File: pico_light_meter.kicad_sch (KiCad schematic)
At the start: 5 parts

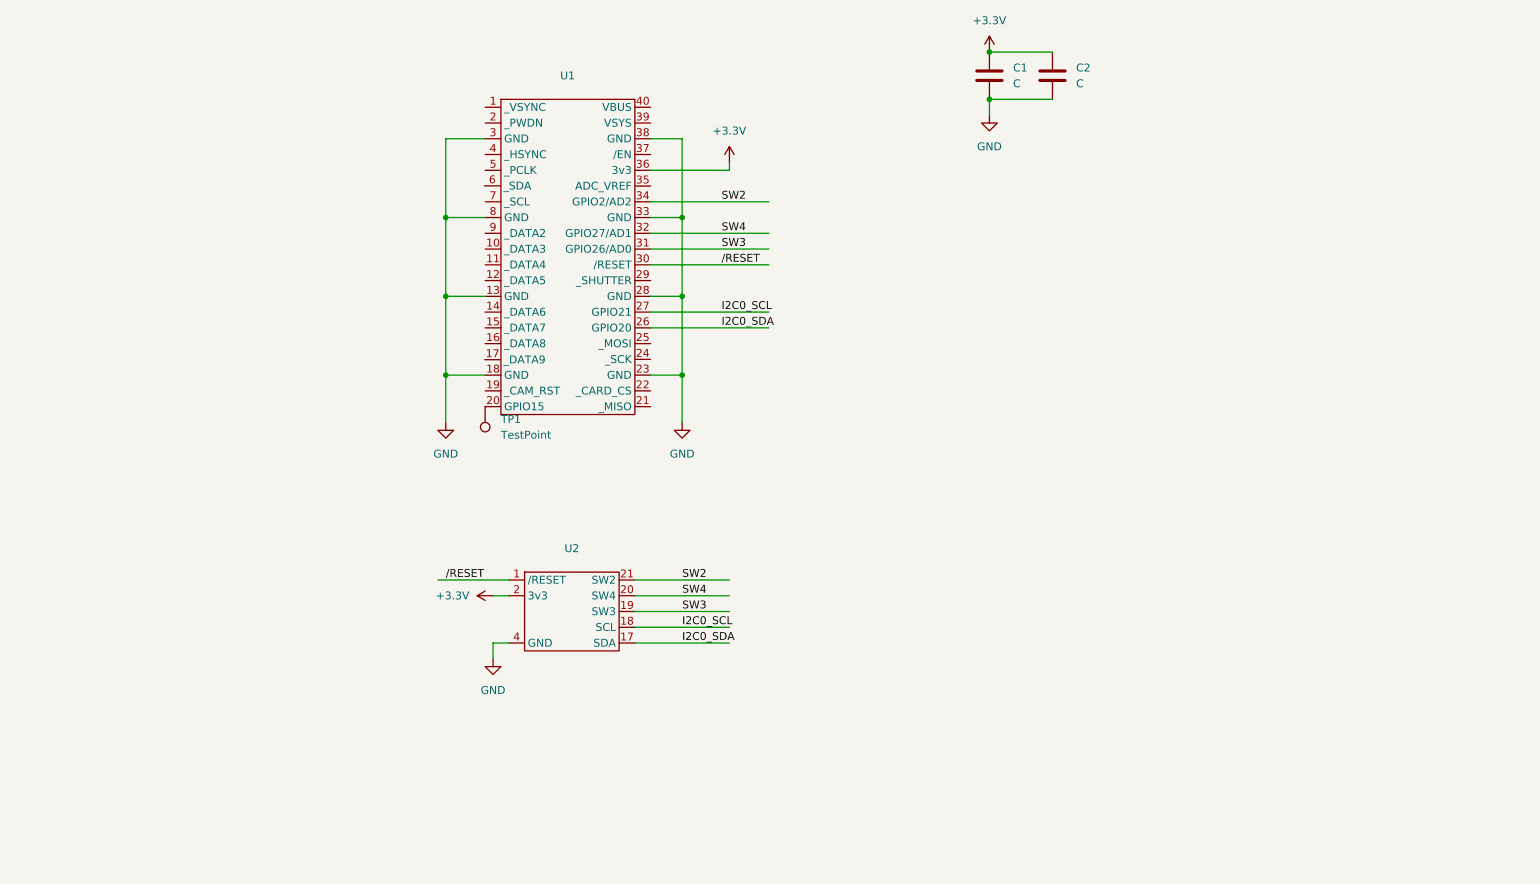
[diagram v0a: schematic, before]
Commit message: Intermediate commit of routed board with Pico on top.
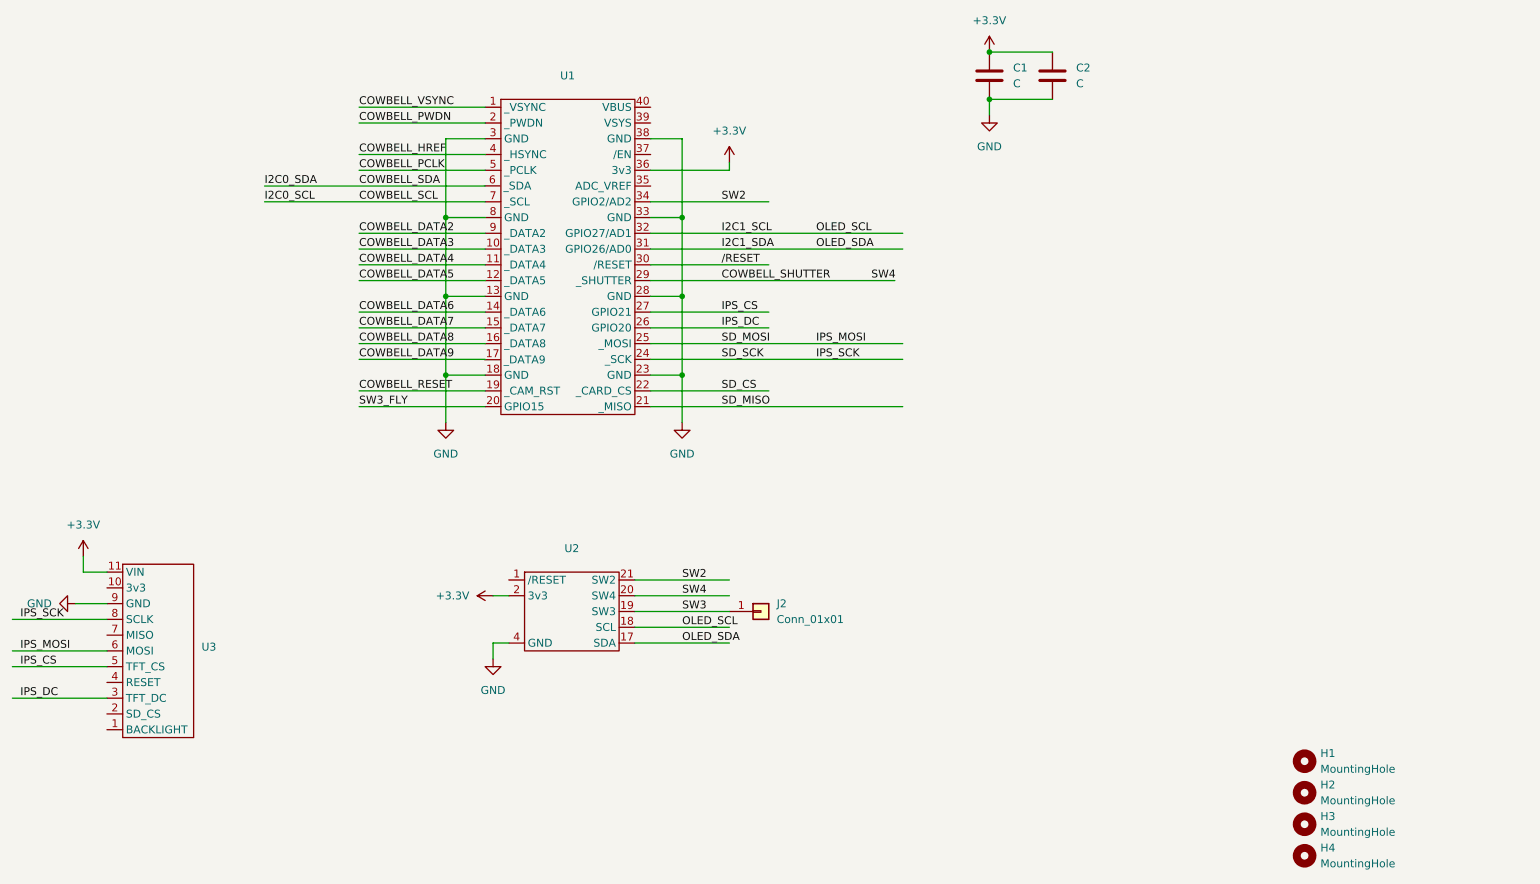
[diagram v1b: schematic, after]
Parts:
- removed TP1: TestPoint, TestPoint:TestPoint_THTPad_D2.0mm_Drill1.0mm, symbol Connector:TestPoint
- added H1, H2, H3, H4: MountingHole, MountingHole:MountingHole_3.2mm_M3_ISO14580, symbol Mechanical:MountingHole
- added J2: Conn_01x01, Connector_PinHeader_1.27mm:PinHeader_1x01_P1.27mm_Vertical, symbol Connector_Generic:Conn_01x01
- added U3: ~, pico_light_meter:adafruit_2.0_IPS_Display, symbol pico_light_meter:Adafruit_2.0_IPS_Display
- U1: footprint pico_light_meter:pico2 -> pico_light_meter:pico2_right_pins_only
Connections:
- net +3.3V: now also U3.11 (VIN)
- net GND: now also U3.9 (GND)
- net SW3: now also J2.1 (Pin_1); no longer U1.31 (GPIO26/AD0)
- net /RESET: no longer U2.1 (/RESET)
- net COWBELL_VSYNC: now reaches U1.1 (_VSYNC)
- net COWBELL_DATA3: now reaches U1.10 (_DATA3)
- net COWBELL_DATA4: now reaches U1.11 (_DATA4)
- net COWBELL_DATA5: now reaches U1.12 (_DATA5)
- net COWBELL_DATA6: now reaches U1.14 (_DATA6)
- net COWBELL_DATA7: now reaches U1.15 (_DATA7)
- net COWBELL_DATA8: now reaches U1.16 (_DATA8)
- net COWBELL_RESET: now reaches U1.19 (_CAM_RST)
- net COWBELL_PWDN: now reaches U1.2 (_PWDN)
- net SW3_FLY: now reaches U1.20 (GPIO15)
- net SD_MISO: now reaches U1.21 (_MISO)
- net SD_CS: now reaches U1.22 (_CARD_CS)
- net IPS_SCK: now reaches U1.24 (_SCK)
- net IPS_SCK: now also U3.8 (SCLK)
- net IPS_MOSI: now reaches U1.25 (_MOSI)
- net IPS_MOSI: now also U3.6 (MOSI)
- net COWBELL_SHUTTER: now reaches U1.29 (_SHUTTER)
- net COWBELL_SHUTTER: now also U2.20 (SW4)
- net COWBELL_HREF: now reaches U1.4 (_HSYNC)
- net COWBELL_PCLK: now reaches U1.5 (_PCLK)
- net COWBELL_SCL: now reaches U1.7 (_SCL)
- net COWBELL_DATA2: now reaches U1.9 (_DATA2)
- net I2C0_SCL renamed I2C1_SCL
- net I2C1_SCL: now also U1.32 (GPIO27/AD1); no longer U1.27 (GPIO21)
- net I2C0_SDA renamed I2C1_SDA
- net I2C1_SDA: now also U1.31 (GPIO26/AD0); no longer U1.26 (GPIO20)
- removed net SW4: U1.32 (GPIO27/AD1), U2.20 (SW4)
- new net IPS_CS: U1.27 (GPIO21), U3.5 (TFT_CS)
- new net IPS_DC: U1.26 (GPIO20), U3.3 (TFT_DC)

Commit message: Updated with MCP port expander
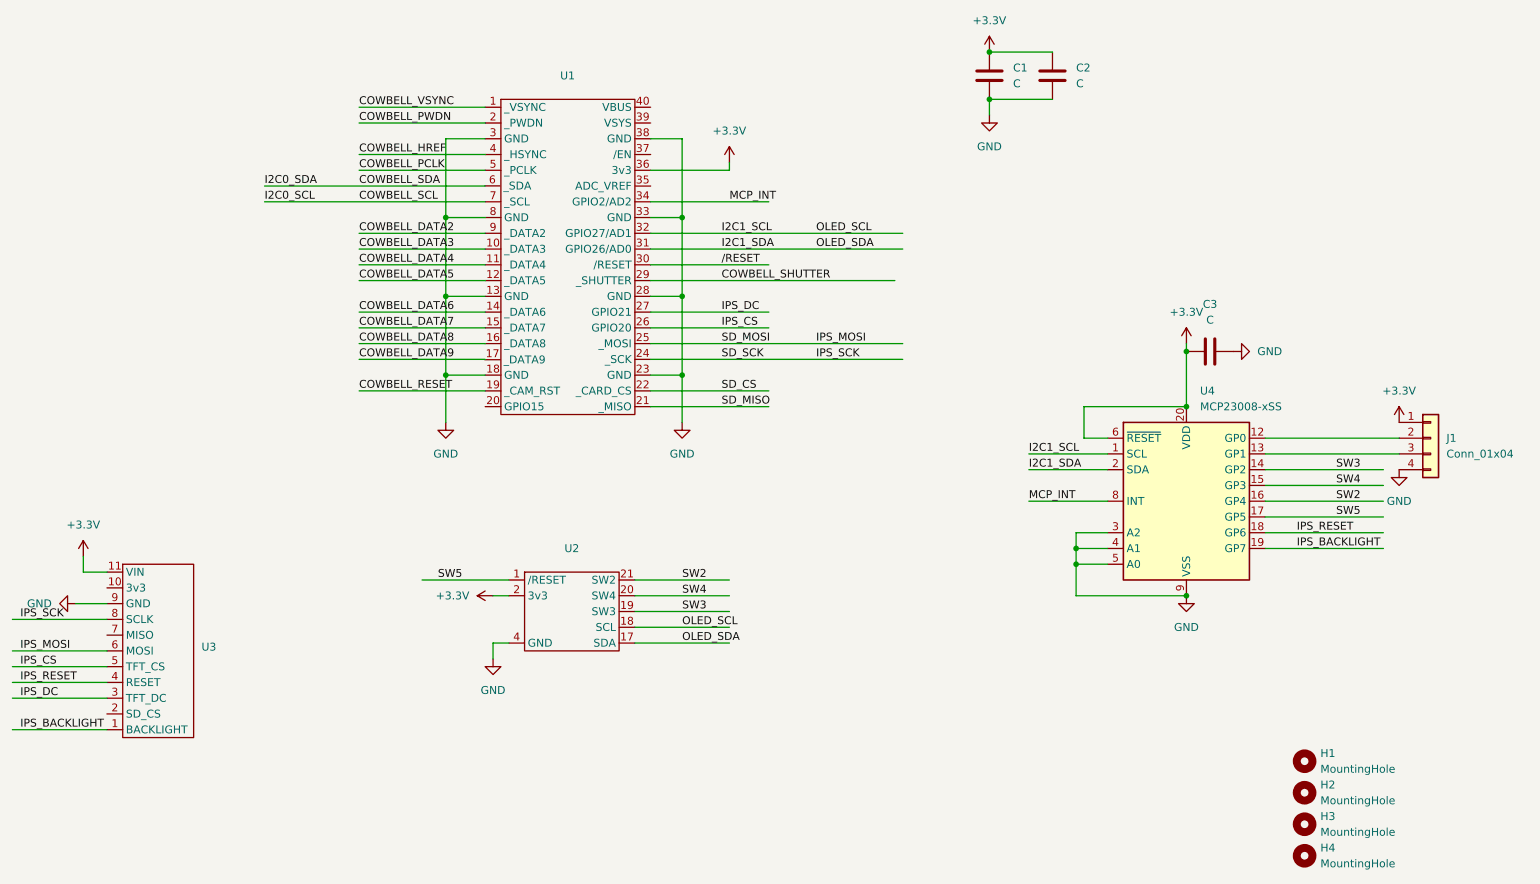
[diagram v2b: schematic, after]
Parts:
- removed J2: Conn_01x01, Connector_PinHeader_1.27mm:PinHeader_1x01_P1.27mm_Vertical, symbol Connector_Generic:Conn_01x01
- added C3: C, Capacitor_SMD:C_0805_2012Metric_Pad1.18x1.45mm_HandSolder, symbol Device:C
- added J1: Conn_01x04, Connector_PinHeader_2.54mm:PinHeader_1x04_P2.54mm_Vertical, symbol Connector_Generic:Conn_01x04
- added U4: MCP23008-xSS, Package_SO:SSOP-20_5.3x7.2mm_P0.65mm, symbol Interface_Expansion:MCP23008-xSS
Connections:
- net +3.3V: now also C3.1, J1.1 (Pin_1), U4.20 (VDD), U4.6 (~{RESET})
- net COWBELL_SHUTTER: no longer U2.20 (SW4)
- net GND: now also C3.2, J1.4 (Pin_4), U4.3 (A2), U4.4 (A1), U4.5 (A0), U4.9 (VSS)
- net I2C1_SCL: now also U4.1 (SCL)
- net I2C1_SDA: now also U4.2 (SDA)
- net IPS_CS: now also U1.26 (GPIO20); no longer U1.27 (GPIO21)
- net IPS_DC: now also U1.27 (GPIO21); no longer U1.26 (GPIO20)
- net SW2: now also U4.16 (GP4); no longer U1.34 (GPIO2/AD2)
- net SW3: now also U4.14 (GP2)
- net SW5: now reaches U2.1 (/RESET)
- net SW5: now also U4.17 (GP5)
- net IPS_BACKLIGHT: now reaches U3.1 (BACKLIGHT)
- net IPS_BACKLIGHT: now also U4.19 (GP7)
- net IPS_RESET: now reaches U3.4 (RESET)
- net IPS_RESET: now also U4.18 (GP6)
- net SW3_FLY: no longer names the net of U1.20 (GPIO15)
- new net: J1.2 (Pin_2), U4.12 (GP0)
- new net: J1.3 (Pin_3), U4.13 (GP1)
- new net MCP_INT: U1.34 (GPIO2/AD2), U4.8 (INT)
- new net SW4: U2.20 (SW4), U4.15 (GP3)

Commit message: Big update to board
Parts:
- U3: footprint pico_light_meter:adafruit_2.0_IPS_Display -> pico_light_meter:adafruit_2.0_IPS_Display_minimal
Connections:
- net IPS_BACKLIGHT: now also U4.15 (GP3); no longer U4.19 (GP7)
- net IPS_CS: now also U1.27 (GPIO21); no longer U1.26 (GPIO20)
- net IPS_DC: now also U1.26 (GPIO20); no longer U1.27 (GPIO21)
- net IPS_RESET: now also U4.14 (GP2); no longer U4.18 (GP6)
- net SW2: now also U4.18 (GP6); no longer U4.16 (GP4)
- net SW3: now also U4.16 (GP4); no longer U4.14 (GP2)
- net SW4: now also U4.17 (GP5); no longer U4.15 (GP3)
- net SW5: now also U4.19 (GP7); no longer U4.17 (GP5)
- net at J1.2 (Pin_2): now also U4.13 (GP1); no longer U4.12 (GP0)
- net at J1.3 (Pin_3): now also U4.12 (GP0); no longer U4.13 (GP1)
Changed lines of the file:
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@@
+	(wire
+		(pts
+			(xy 266.7 95.25) (xy 266.7 91.44)
+		)
+		(stroke
+			(width 0)
+			(type default)
+		)
+	)
 	(wire
 		(pts
@@
 	(wire
 		(pts
+			(xy 261.62 91.44) (xy 261.62 92.71)
+		)
+		(stroke
+			(width 0)
+			(type default)
+		)
+	)
+	(wire
+		(pts
 			(xy 154.94 123.19) (xy 170.18 123.19)
 		)
@@
 	(wire
 		(pts
-			(xy 256.54 95.25) (xy 278.13 95.25)
-		)
-		(stroke
-			(width 0)
-			(type default)
-		)
-	)
-	(wire
-		(pts
 			(xy 243.84 78.74) (xy 243.84 87.63)
 		)
@@
 	(wire
 		(pts
+			(xy 278.13 95.25) (xy 266.7 95.25)
+		)
+		(stroke
+			(width 0)
+			(type default)
+		)
+	)
+	(wire
+		(pts
 			(xy 110.49 46.99) (xy 130.81 46.99)
 		)
@@
 	(wire
 		(pts
+			(xy 264.16 95.25) (xy 264.16 92.71)
+		)
+		(stroke
+			(width 0)
+			(type default)
+		)
+	)
+	(wire
+		(pts
 			(xy 130.81 80.01) (xy 110.49 80.01)
 		)
@@
 	(wire
 		(pts
+			(xy 266.7 91.44) (xy 261.62 91.44)
+		)
+		(stroke
+			(width 0)
+			(type default)
+		)
+	)
+	(wire
+		(pts
 			(xy 66.04 111.76) (xy 66.04 114.3)
 		)
@@
 	(wire
 		(pts
+			(xy 261.62 92.71) (xy 256.54 92.71)
+		)
+		(stroke
+			(width 0)
+			(type default)
+		)
+	)
+	(wire
+		(pts
 			(xy 212.09 38.1) (xy 222.25 38.1)
 		)
@@
 	(wire
 		(pts
+			(xy 264.16 92.71) (xy 278.13 92.71)
+		)
+		(stroke
+			(width 0)
+			(type default)
+		)
+	)
+	(wire
+		(pts
 			(xy 64.77 119.38) (xy 69.85 119.38)
 		)
@@
 	(wire
 		(pts
+			(xy 256.54 95.25) (xy 264.16 95.25)
+		)
+		(stroke
+			(width 0)
+			(type default)
+		)
+	)
+	(wire
+		(pts
 			(xy 162.56 82.55) (xy 162.56 69.85)
 		)
@@
 		(pts
 			(xy 226.06 118.11) (xy 243.84 118.11)
-		)
-		(stroke
-			(width 0)
-			(type default)
-		)
-	)
-	(wire
-		(pts
-			(xy 256.54 92.71) (xy 278.13 92.71)
 		)
 		(stroke
@@
 	)
 	(label "IPS_RESET"
-		(at 261.62 107.95 0)
+		(at 262.89 97.79 0)
 		(effects
 			(font
@@
 	)
 	(label "IPS_CS"
-		(at 168.91 74.93 0)
+		(at 168.91 72.39 0)
 		(effects
 			(font
@@
 	)
 	(label "SW3"
-		(at 267.97 97.79 0)
+		(at 267.97 102.87 0)
 		(effects
 			(font
@@
 	)
 	(label "IPS_DC"
-		(at 168.91 72.39 0)
+		(at 168.91 74.93 0)
 		(effects
 			(font
@@
 	)
 	(label "SW5"
-		(at 267.97 105.41 0)
+		(at 267.97 110.49 0)
 		(effects
 			(font
@@
 	)
 	(label "IPS_BACKLIGHT"
-		(at 261.62 110.49 0)
+		(at 262.89 100.33 0)
 		(effects
 			(font
@@
 	)
 	(label "SW2"
-		(at 267.97 102.87 0)
+		(at 267.97 107.95 0)
 		(effects
 			(font
@@
 	)
 	(label "SW4"
-		(at 267.97 100.33 0)
+		(at 267.97 105.41 0)
 		(effects
 			(font
@@
 			)
 		)
-		(property "Footprint" "pico_light_meter:adafruit_2.0_IPS_Display"
+		(property "Footprint" "pico_light_meter:adafruit_2.0_IPS_Display_minimal"
 			(at 72.39 113.03 0)
 			(effects
